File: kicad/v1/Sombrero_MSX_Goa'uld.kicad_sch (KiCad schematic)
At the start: 16 parts, among them J1 Z80CPU, U1 74HCT373, U2 74HCT373, U3 SN74LVC245AN, U4 SN74LVC245AN, U5 SN74LVC245AN, U6 Tang_Nano_20k

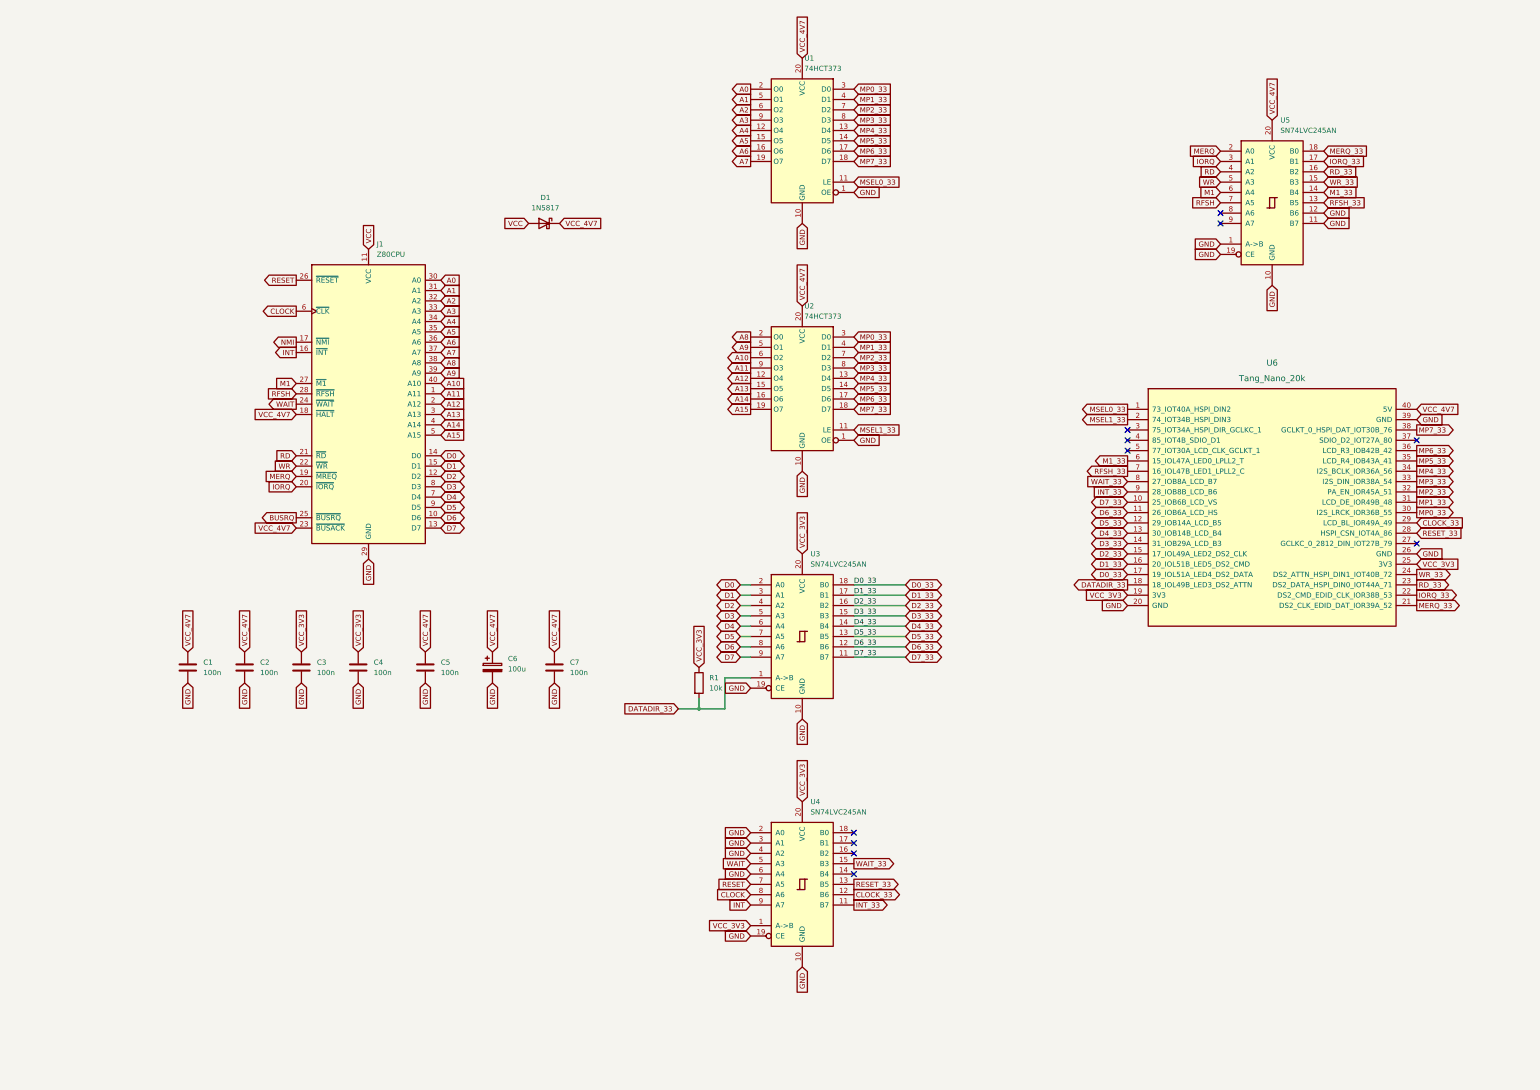
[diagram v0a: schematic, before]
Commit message: HW Version 1.4 -Included resistor array -Replaced U1, U2 -> 74HC373, U5 -> 74HC245 -Removed capacitor, resistor -Reduced size
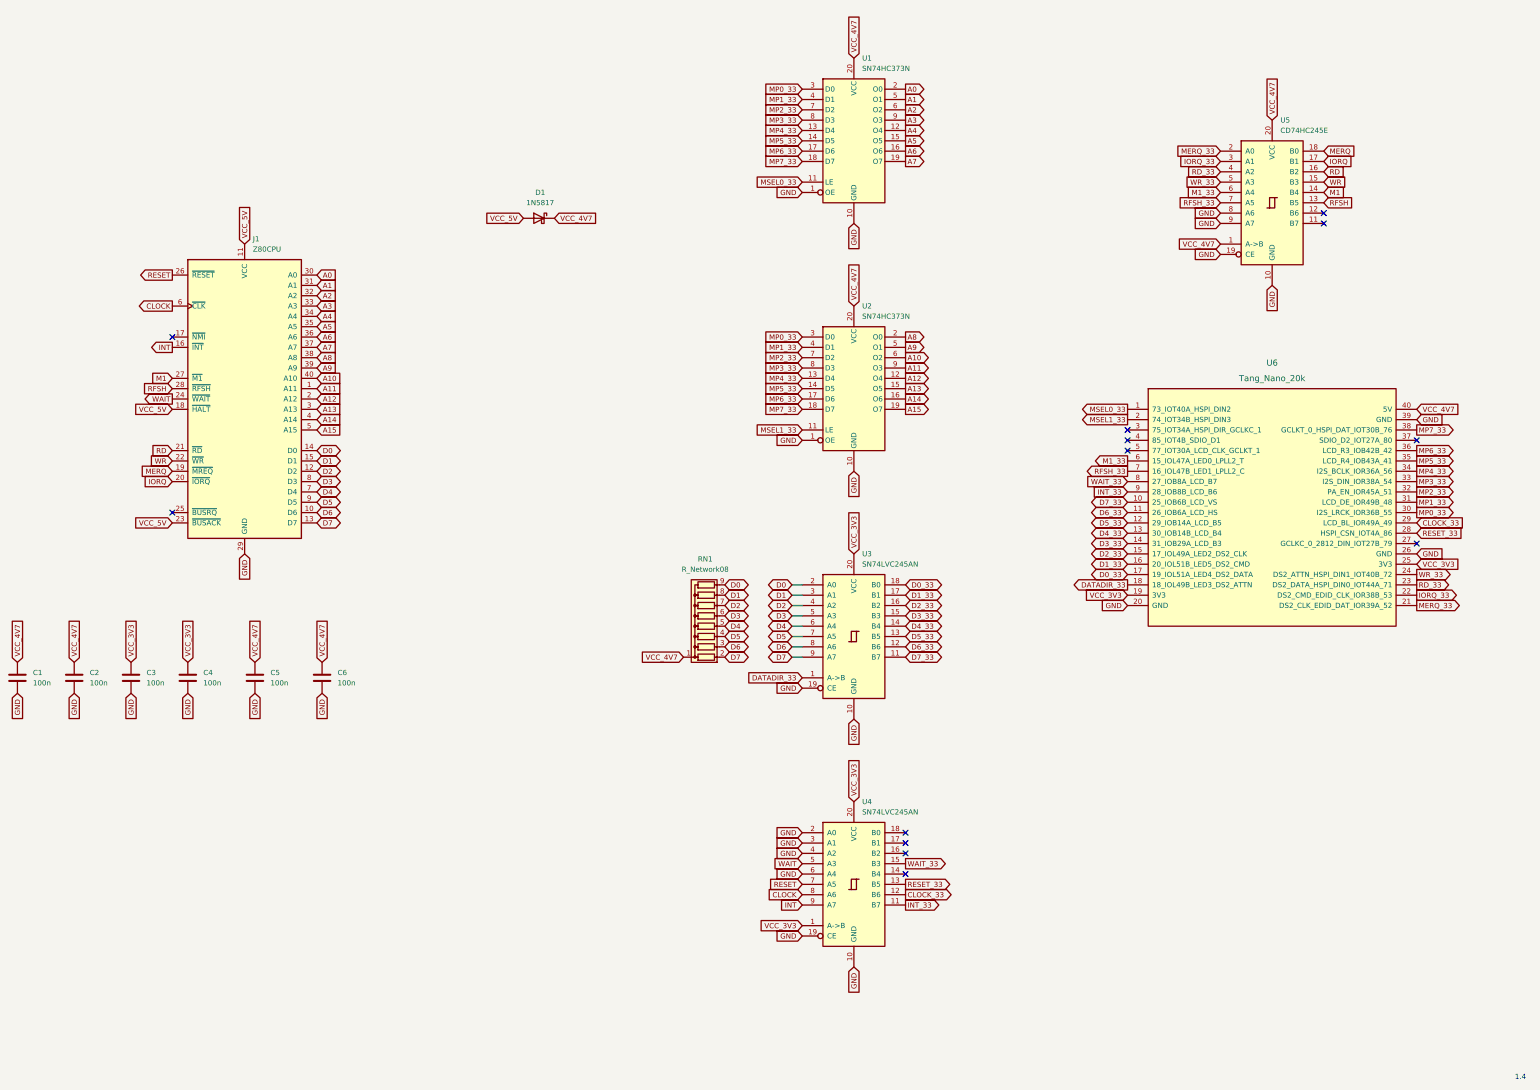
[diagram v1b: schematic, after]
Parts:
- removed C6: 100u, Capacitor_THT:CP_Radial_D8.0mm_P3.50mm, symbol Device:C_Polarized
- removed R1: 10k, Resistor_THT:R_Axial_DIN0207_L6.3mm_D2.5mm_P7.62mm_Horizontal, symbol Device:R
- removed U1, U2: 74HCT373, Package_DIP:DIP-20_W7.62mm_LongPads, symbol 74xx:74AHCT373
- removed U5: SN74LVC245AN, Package_DIP:DIP-20_W7.62mm_LongPads, symbol Mi_libreria:SN74LVC245AN
- added RN1: R_Network08, Resistor_THT:R_Array_SIP9, symbol Device:R_Network08
- added U1, U2: SN74HC373N, Package_DIP:DIP-20_W7.62mm_LongPads, symbol 74xx:74HC373
- added U5: CD74HC245E, Package_DIP:DIP-20_W7.62mm_LongPads, symbol 74xx:74HC245
- D1: footprint Diode_THT:D_DO-41_SOD81_P10.16mm_Horizontal -> Diode_THT:D_DO-41_SOD81_P7.62mm_Horizontal
- renumbered C7 to C6
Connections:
- net A0: now also U1.2 (O0)
- net A1: now also U1.5 (O1)
- net A10: now also U2.6 (O2)
- net A11: now also U2.9 (O3)
- net A12: now also U2.12 (O4)
- net A13: now also U2.15 (O5)
- net A14: now also U2.16 (O6)
- net A15: now also U2.19 (O7)
- net A2: now also U1.6 (O2)
- net A3: now also U1.9 (O3)
- net A4: now also U1.12 (O4)
- net A5: now also U1.15 (O5)
- net A6: now also U1.16 (O6)
- net A7: now also U1.19 (O7)
- net A8: now also U2.2 (O0)
- net A9: now also U2.5 (O1)
- net D0: now also RN1.9 (R8)
- net D1: now also RN1.8 (R7)
- net D2: now also RN1.7 (R6)
- net D3: now also RN1.6 (R5)
- net D4: now also RN1.5 (R4)
- net D5: now also RN1.4 (R3)
- net D6: now also RN1.3 (R2)
- net D7: now also RN1.2 (R1)
- net GND: now also U1.1 (OE), U1.10 (GND), U2.1 (OE), U2.10 (GND), U5.10 (GND), U5.19 (CE), U5.8 (A6), U5.9 (A7)
- net IORQ: now also U5.17 (B1)
- net IORQ_33: now also U5.3 (A1)
- net M1: now also U5.14 (B4)
- net M1_33: now also U5.6 (A4)
- net MERQ: now also U5.18 (B0)
- net MERQ_33: now also U5.2 (A0)
- net MP0_33: now also U1.3 (D0), U2.3 (D0)
- net MP1_33: now also U1.4 (D1), U2.4 (D1)
- net MP2_33: now also U1.7 (D2), U2.7 (D2)
- net MP3_33: now also U1.8 (D3), U2.8 (D3)
- net MP4_33: now also U1.13 (D4), U2.13 (D4)
- net MP5_33: now also U1.14 (D5), U2.14 (D5)
- net MP6_33: now also U1.17 (D6), U2.17 (D6)
- net MP7_33: now also U1.18 (D7), U2.18 (D7)
- net MSEL0_33: now also U1.11 (LE)
- net MSEL1_33: now also U2.11 (LE)
- net RD: now also U5.16 (B2)
- net RD_33: now also U5.4 (A2)
- net RFSH: now also U5.13 (B5)
- net RFSH_33: now also U5.7 (A5)
- net VCC_4V7: now also RN1.1 (common), U1.20 (VCC), U2.20 (VCC), U5.1 (A->B), U5.20 (VCC); no longer J1.18 (~{HALT}), J1.23 (~{BUSACK})
- net WR: now also U5.15 (B3)
- net WR_33: now also U5.5 (A3)
- net BUSRQ: no longer names the net of J1.25 (~{BUSRQ})
- net NMI: no longer names the net of J1.17 (~{NMI})
- net VCC renamed VCC_5V
- net VCC_5V: now also J1.18 (~{HALT}), J1.23 (~{BUSACK})
- no-connect marks 11 -> 13
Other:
- note added: "1.4"
- moved on the sheet: C1, C2, C3, C4, C5, C6, J1, U3, U4
